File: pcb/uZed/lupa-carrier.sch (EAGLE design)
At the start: 56 parts, among them K1 694108105102

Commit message: layout out power for lupa
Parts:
- removed C20, C21, C4: 0.1uF, rcl:C-EUC0603
- removed C5: .1uF, rcl:C-EUC0603
- removed R19: 110k, rcl:R-US_R0603
- removed R20: 42k, rcl:R-US_R0603
- removed R21: 1.5M, rcl:R-US_R0603
- removed R22: 500k, rcl:R-US_R0603
- removed R5: 68k, rcl:R-US_R0603
- removed R6: 10k, rcl:R-US_R0603
- added C22, C23, C26, C27: (no value), rcl:C-EUC0603
- added C24, C25: .1uf, rcl:C-EUC0603
- added C29: 10uF, rcl:C-USC0603
- added C30, C31: 1uF, rcl:C-USC0603
- added R23: 68k, rcl:R-US_R0603
- added R24: 10k, rcl:R-US_R0603
- added R25: 110k, rcl:R-US_R0603
- added R26: 42k, rcl:R-US_R0603
- added R27: 1.5M, rcl:R-US_R0603
- added R28: 500k, rcl:R-US_R0603
- added U$5: ADP7158ARDZ-2.5-R7CT-ND, lupa300-components:ADP7158ARDZ-2.5-R7CT-ND
- added U$6: XC6210B252MR-G, lupa300-components:XC6210B252MR-G
- C6: value 0.1uF -> 10uF; device rcl:C-EUC0603 -> rcl:C-USC0603
- C7: value 0.1uF -> 1uF; device rcl:C-EUC0603 -> rcl:C-USC0603
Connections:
- net SPI_CLK renamed CPI_CLK
- net VRESET_1 renamed VRESET1
- net VRESET_2 renamed VRESET2
- net VRESET_3 renamed VRESET3
- new net GNDA: C24.1, C25.1, C26.1, C27.1, C29.2, C30.2, C31.2, C6.2, C7.2, U$4.GNDA, U$4.GNDA1, U$4.GNDA2, U$5.GND
- new net GNDADC: C23.1, U$4.GNDADC, U$4.GNDADC1
- new net GNDD: U$4.GNDD, U$4.GNDD1, U$6.GND
- new net GNDO: U$4.GNDO
- new net GND_DRIVERS: C22.1, U$4.GND_DRIVERS
- new net N$14: C7.1, U$5.BYP
- new net N$22: C30.1, U$5.VREG
- new net N$23: C31.1, U$5.REF, U$5.REF_SEN
- new net N$3: C6.1, U$5.VOUT, U$5.VO_SEN
- new net VDDA_EN: U$5.EN
- new net VDDD_EN: U$6.EN
- net 5V: now also C29.1, U$5.VIN, U$6.VIN
- net ADC_BIAS: now also C23.2, R24.1; no longer C4.1, R6.2
- net BIAS1: now also C27.2, R28.1; no longer C21.1, R22.2
- net BIAS2: now also C26.2, R27.1; no longer C20.1, R21.2
- net BIAS3: now also C25.2, R26.1; no longer C6.1, R20.2
- net BIAS4: now also C24.2, R25.1; no longer C5.1, R19.2
- net GND: no longer C20.2, C21.2, C4.2, C5.2, C6.2, C7.2, U$4.GNDA, U$4.GNDA1, U$4.GNDA2, U$4.GNDADC, U$4.GNDADC1, U$4.GNDD, U$4.GNDD1, U$4.GNDO, U$4.GND_DRIVERS
- net PRECHARGE_BIAS: now also C22.2, R23.1; no longer C7.1, R5.2
- net VADC: now also R24.2; no longer R6.1
- net VDDA: now also R25.2, R26.2, R27.2, R28.2; no longer R19.1, R20.1, R21.1, R22.1
- net VDDD: now also U$6.VOUT
- net VPIX: now also R23.2; no longer R5.1

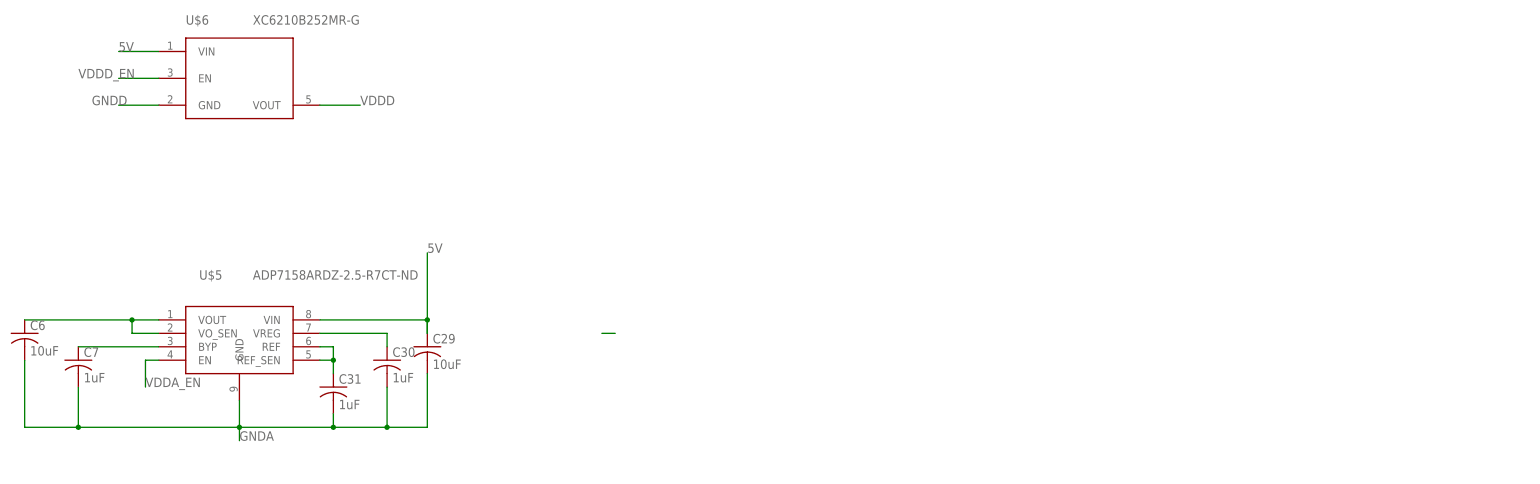
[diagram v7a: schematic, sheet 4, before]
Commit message: added low noise regulators for sensitive lupa supplys
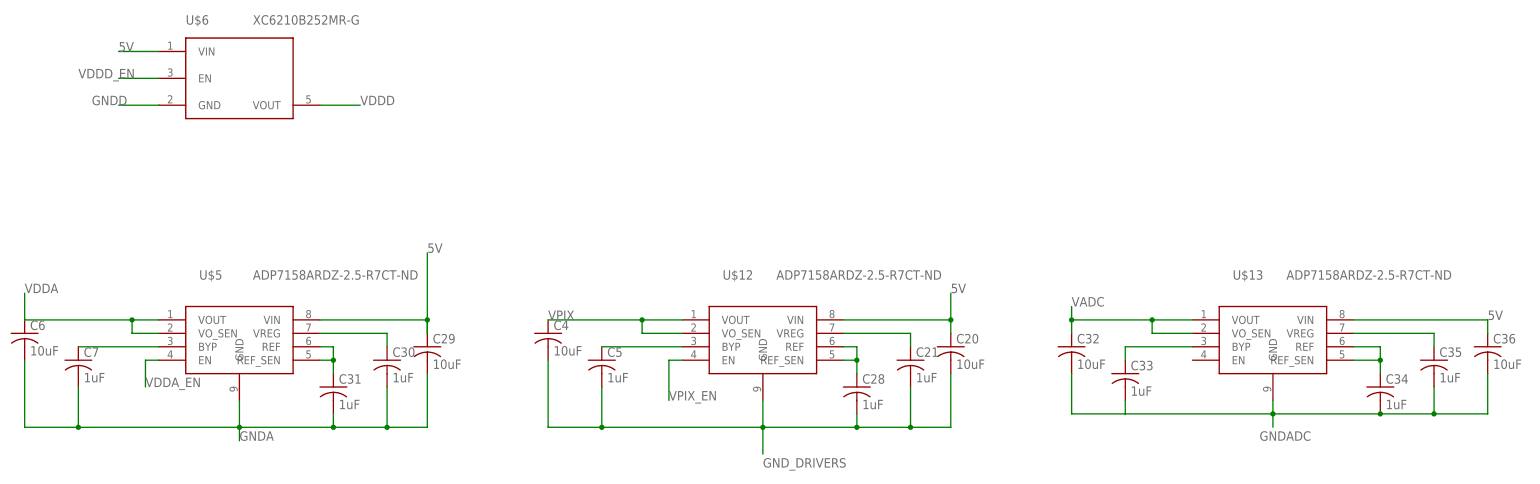
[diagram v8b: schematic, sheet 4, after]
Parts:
- added C20, C32, C36, C4: 10uF, rcl:C-USC0603
- added C21, C28, C33, C34, C35, C5: 1uF, rcl:C-USC0603
- added U$12, U$13: ADP7158ARDZ-2.5-R7CT-ND, lupa300-components:ADP7158ARDZ-2.5-R7CT-ND
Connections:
- new net N$13: C28.1, U$12.REF, U$12.REF_SEN
- new net N$18: C35.1, U$13.VREG
- new net N$19: C34.1, U$13.REF, U$13.REF_SEN
- new net N$2: C5.1, U$12.BYP
- new net N$20: C33.1, U$13.BYP
- new net VPIX_EN: U$12.EN
- net 5V: now also C20.1, C36.1, U$12.VIN, U$13.VIN
- net GNDADC: now also C32.2, C33.2, C34.2, C35.2, C36.2, U$13.GND
- net GND_DRIVERS: now also C20.2, C21.2, C28.2, C4.2, C5.2, U$12.GND
- net N$3: now also C21.1, U$12.VREG; no longer C6.1, U$5.VOUT, U$5.VO_SEN
- net VADC: now also C32.1, U$13.VOUT, U$13.VO_SEN
- net VDDA: now also C6.1, U$5.VOUT, U$5.VO_SEN
- net VPIX: now also C4.1, U$12.VOUT, U$12.VO_SEN
